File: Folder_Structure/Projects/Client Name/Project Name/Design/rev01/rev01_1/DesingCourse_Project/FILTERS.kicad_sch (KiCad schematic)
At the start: 0 parts

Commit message: Update 6
SCH and LIB for MOSFET page done, missing passive components
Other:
- company: (none) -> Integro Consulting AB
- title: (none) -> PCB Mastery Project
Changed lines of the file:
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@@
 	(generator_version "9.0")
 	(paper "A4")
+	(title_block
+		(title "PCB Mastery Project")
+		(date "2026-01-27")
+		(rev "001")
+		(company "Integro Consulting AB")
+		(comment 1 "TBD")
+		(comment 2 "TBD")
+		(comment 3 "TBD")
+		(comment 4 "Josue Godinez")
+	)
 )

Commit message: Update 11
SCH finishe, missing the labels and logos and adding all passive components
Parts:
- added C53, C56, C58, C60: 100n, symbol Device:C
- added C54, C55, C57, C59: 4n7, symbol Device:C
- added J10: 874380643, 874380843:MOLEX_874380643, symbol Molex_87438:874380643
- added R52, R55, R57, R59: 10k, symbol Device:R
- added R53: 0R, symbol Device:R
- added R54, R56, R58: 2k2, symbol Device:R
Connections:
- new net GND: C53.2, C54.2, C55.2, C56.2, C57.2, C58.2, C59.2, C60.2, J10.6_1 (6), J10.6_2 (6)
- new net HALL1_IN: C55.1, J10.3_1 (3), J10.3_2 (3), R54.2, R55.2
- new net HALL1_OUT: R55.1
- new net HALL2_IN: C57.1, J10.4_1 (4), J10.4_2 (4), R56.2, R57.2
- new net HALL2_OUT: R57.1
- new net HALL3_IN: C59.1, J10.5_1 (5), J10.5_2 (5), R58.2, R59.2
- new net HALL3_OUT: R59.1
- new net P3V3: C53.1, C56.1, C58.1, C60.1, R52.1, R54.1, R56.1, R58.1
- new net P5V: J10.1_1 (1), J10.1_2 (1)
- new net TEMP_IN: C54.1, J10.2_1 (2), J10.2_2 (2), R52.2, R53.2
- new net TEMP_MOTOR: R53.1
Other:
- note added: "FILTERS"
- note added: "HALL_1 FILTER"
- note added: "HALL_2 FILTER"
- note added: "HALL_3 FILTER"
- note added: "INPUT"
- note added: "INPUT HALL ENCODER (TO MCU ==>)"
- note added: "TEMP_MOTOR FILTER"

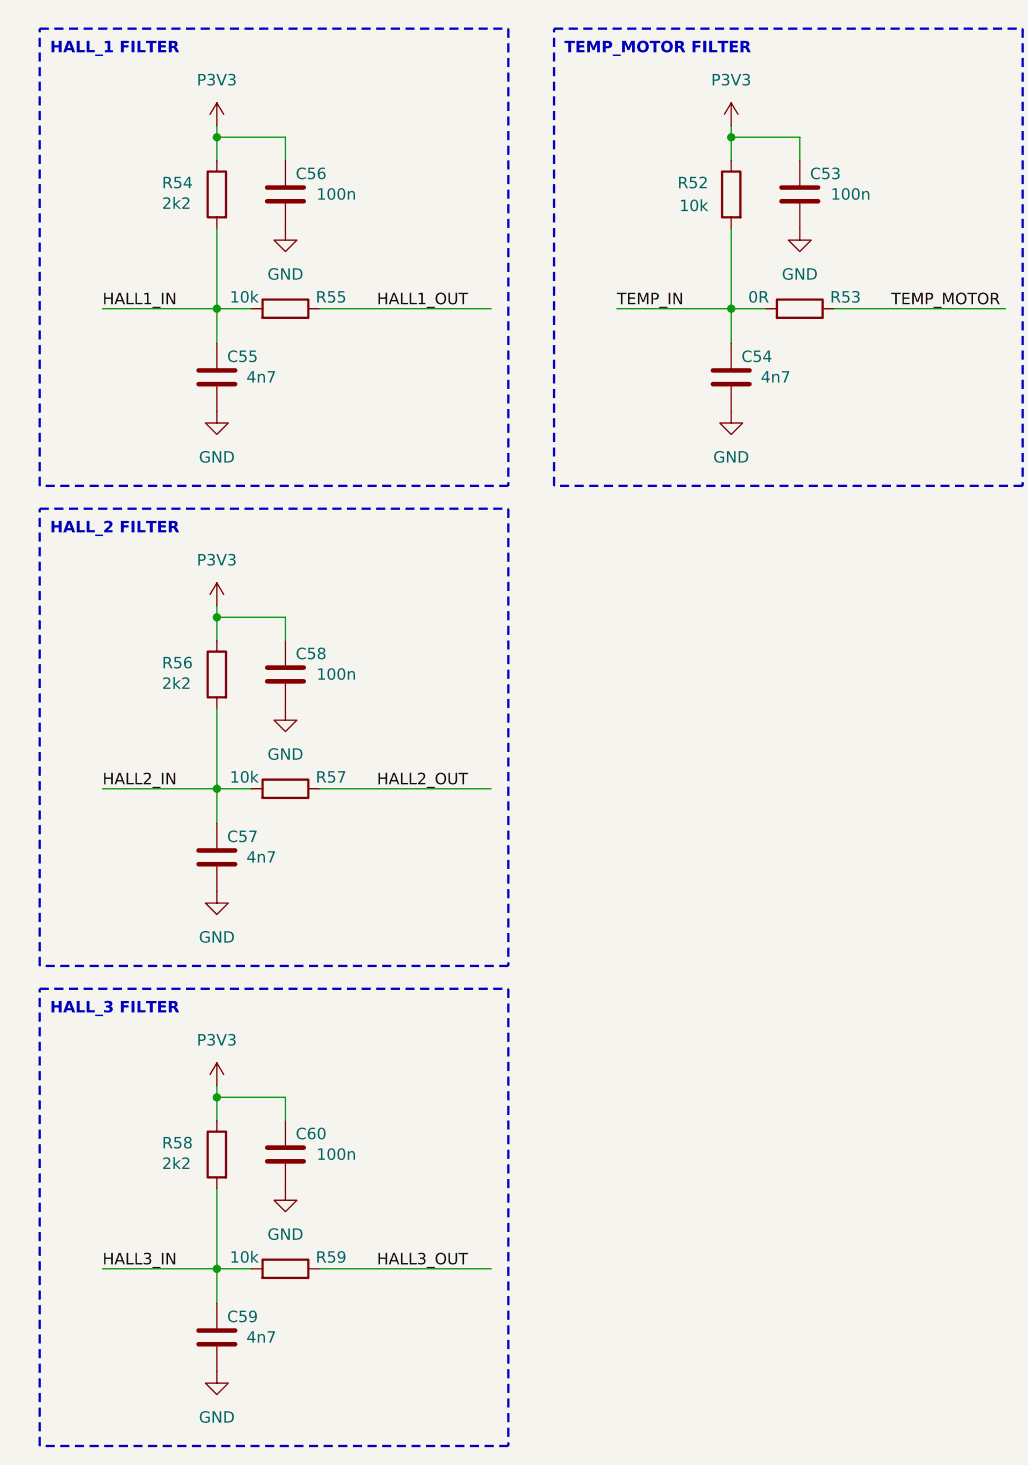
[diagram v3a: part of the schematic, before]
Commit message: Update 12
Until STEP-DOWN page, all components have complete libraries.

Creation and incluison of all logos and labels libraries
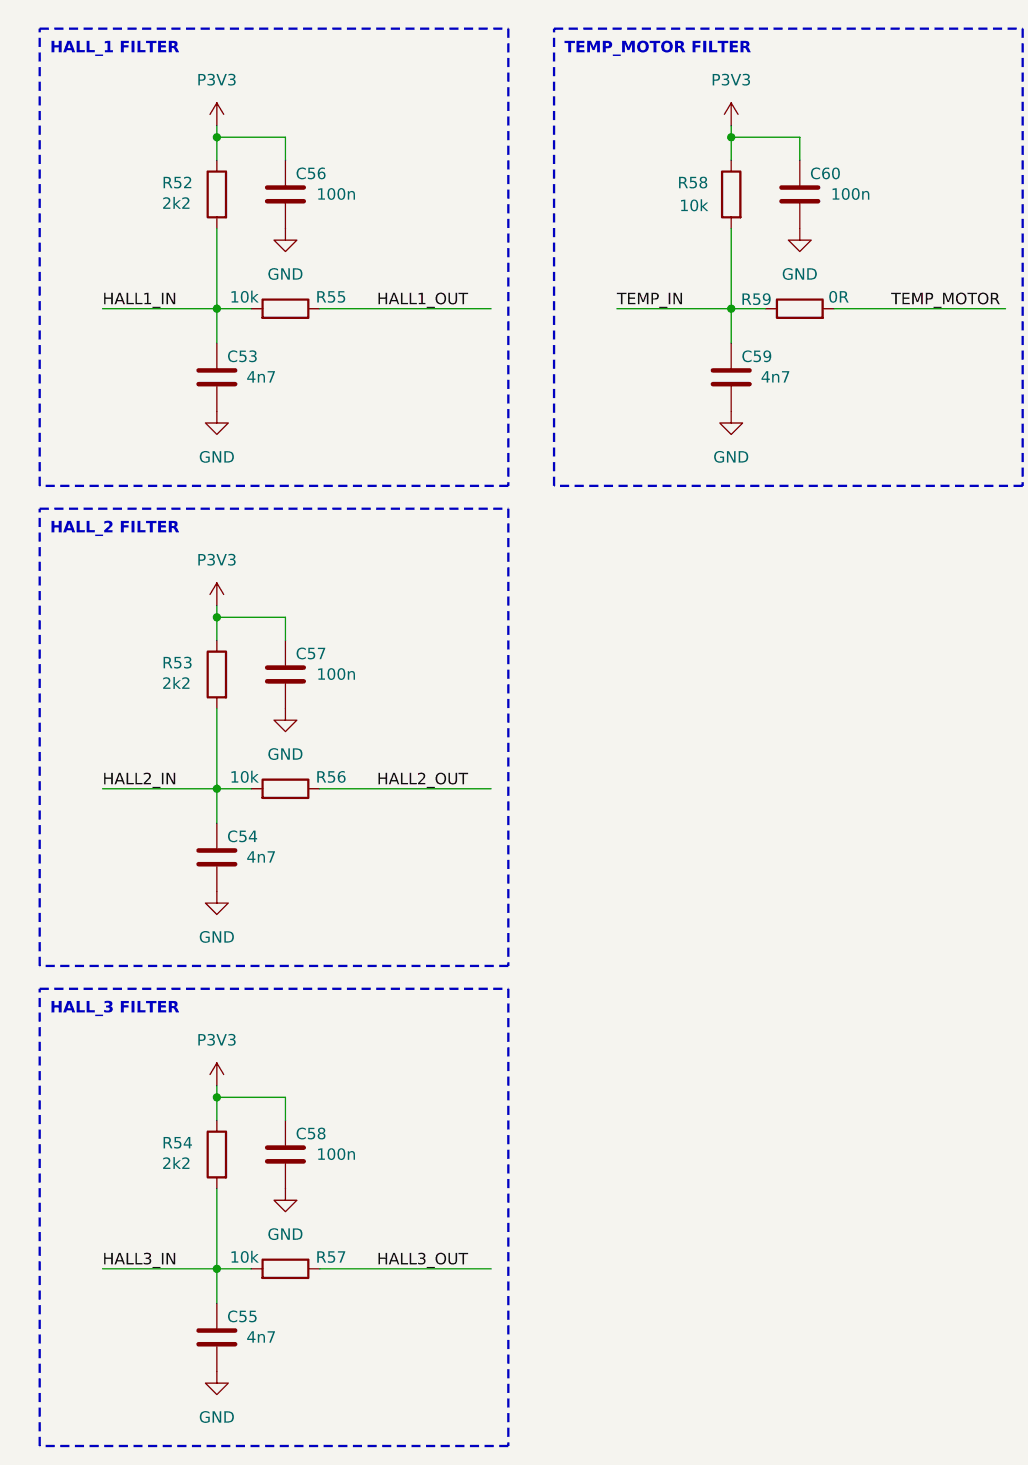
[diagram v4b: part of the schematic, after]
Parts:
- removed R53: 0R, symbol Device:R
- added R59: 0R, Resistor_SMD:R_0603_1608Metric, symbol Device:R
- renumbered C55 to C53, C57 to C54, C59 to C55, C58 to C57, C60 to C58, C54 to C59, C53 to C60, R54 to R52, R56 to R53, R58 to R54, R57 to R56, R59 to R57, R52 to R58
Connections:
- net TEMP_IN: now also R59.1
- net TEMP_MOTOR: now also R59.2

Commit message: Update13
Still working on FP for the MCU
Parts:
- C56, C57, C58, C60: footprint (none) -> Capacitor_SMD:C_0603_1608Metric; Package (none) -> 0603; Temp Coeff (none) -> X7R; Tolerance (none) -> 10%; Voltage Rating (none) -> 10V
- R52, R53, R54: footprint (none) -> Resistor_SMD:R_0603_1608Metric; Package (none) -> 0603; Power Rating (none) -> 1/10W; Tolerance (none) -> 1%

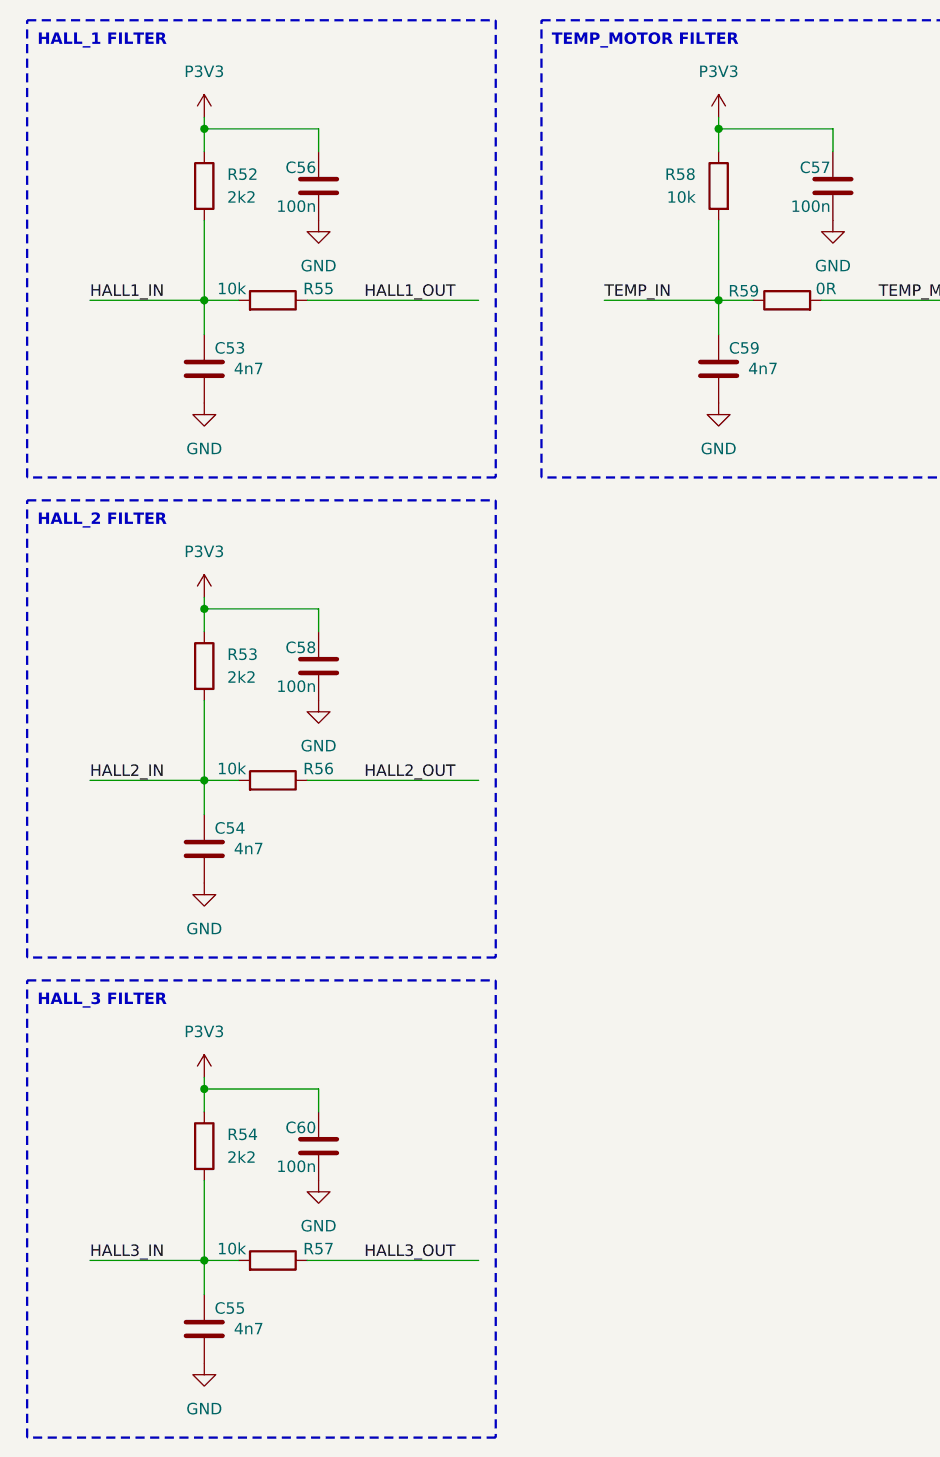
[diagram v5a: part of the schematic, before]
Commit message: Update14
All components with FP, missing the block diagram
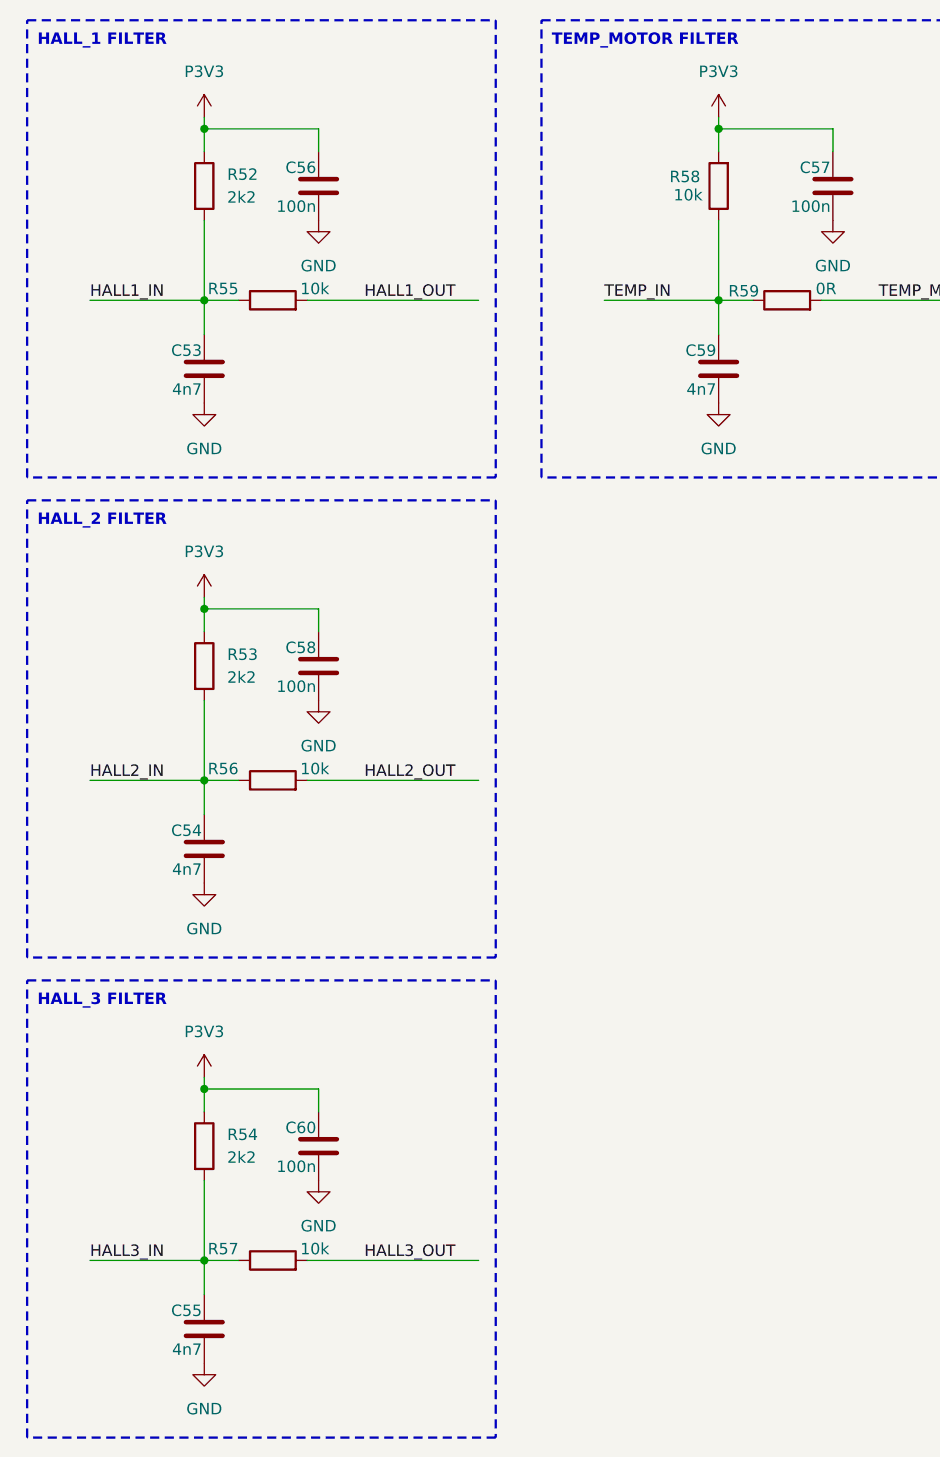
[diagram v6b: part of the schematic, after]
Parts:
- C53, C54, C55, C59: footprint (none) -> Capacitor_SMD:C_0603_1608Metric; Package (none) -> 0603; Temp Coeff (none) -> X7R; Tolerance (none) -> 10%; Voltage Rating (none) -> 50V
- R55, R56, R57, R58: footprint (none) -> Resistor_SMD:R_0603_1608Metric; Package (none) -> 0603; Power Rating (none) -> 1/10W; Tolerance (none) -> 1%
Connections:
- net HALL1_IN: now also R55.1; no longer R55.2
- net HALL1_OUT: now also R55.2; no longer R55.1
- net HALL2_IN: now also R56.1; no longer R56.2
- net HALL2_OUT: now also R56.2; no longer R56.1
- net HALL3_IN: now also R57.1; no longer R57.2
- net HALL3_OUT: now also R57.2; no longer R57.1
- net P3V3: now also R58.2; no longer R58.1
- net TEMP_IN: now also R58.1; no longer R58.2
